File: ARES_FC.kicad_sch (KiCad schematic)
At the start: 65 parts, among them J1 SWD, J2 TYPE-C-31-M-12, J3 FC_M/P, J4 5V, J5 GND, J6 FC_RF, J7 Conn_01x04_Pin, J8 Conn_01x04_Pin, U1 STM32F401CCU6, U2 AMS1117-3.3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

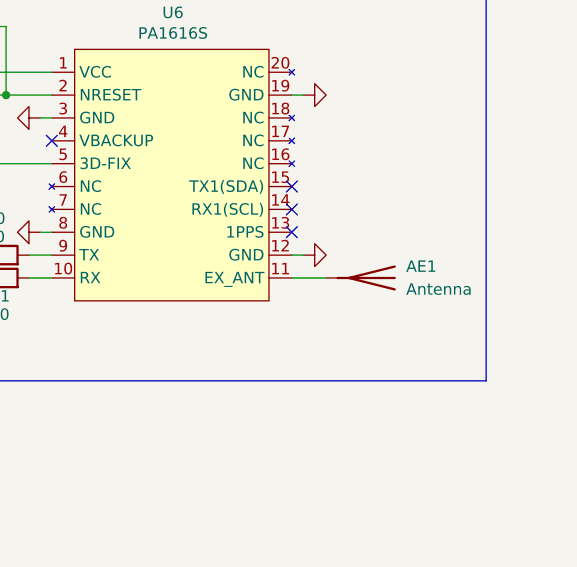
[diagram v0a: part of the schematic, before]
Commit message: added gps antenna shielding
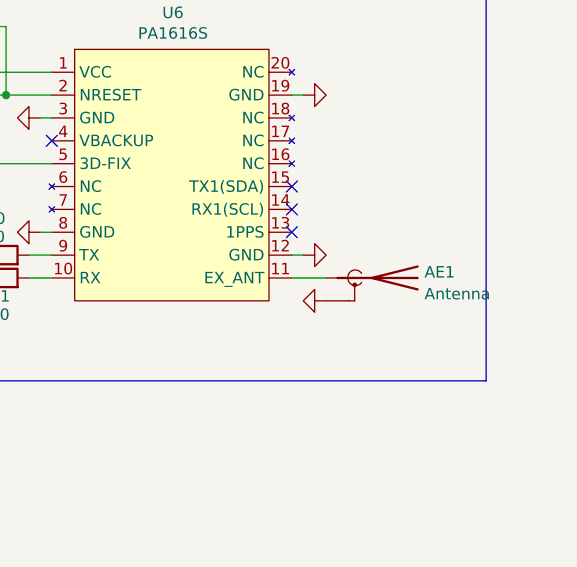
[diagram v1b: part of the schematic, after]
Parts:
- AE1: symbol Device:Antenna -> Device:Antenna_Shield
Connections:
- net GND: now also AE1.2 (Shield)
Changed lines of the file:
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@@
 	)
 	(symbol
-		(lib_id "Device:Antenna")
+		(lib_id "Device:Antenna_Shield")
 		(at 373.38 133.35 270)
 		(unit 1)
@@
 		(fields_autoplaced yes)
 		(property "Reference" "AE1"
-			(at 377.19 132.0799 90)
+			(at 379.222 132.7093 90)
 			(effects
 				(font
@@
 		)
 		(property "Value" "Antenna"
-			(at 377.19 134.6199 90)
+			(at 379.222 135.1336 90)
 			(effects
 				(font
@@
 		)
 		(property "Footprint" "Connector_Coaxial:U.FL_Molex_MCRF_73412-0110_Vertical"
-			(at 373.38 133.35 0)
+			(at 375.92 133.35 0)
 			(effects
 				(font
@@
 		)
 		(property "Datasheet" "~"
-			(at 373.38 133.35 0)
+			(at 375.92 133.35 0)
 			(effects
 				(font
@@
 			)
 		)
-		(property "Description" "Antenna"
+		(property "Description" "Antenna with extra pin for shielding"
 			(at 373.38 133.35 0)
 			(effects
@@
 		(pin "1"
 		)
+		(pin "2"
+		)
 		(instances
 			(project "ARES_FC"
@@
 					(unit 1)
 				)
+			)
+		)
+	)
+	(symbol
+		(lib_id "power:GND")
+		(at 368.3 135.89 270)
+		(unit 1)
+		(exclude_from_sim no)
+		(in_bom yes)
+		(on_board yes)
+		(dnp no)
+		(fields_autoplaced yes)
+		(property "Reference" "#PWR026"
+			(at 361.95 135.89 0)
+			(effects
+				(font
+					(size 1.27 1.27)
+				)
+				(hide yes)
+			)
+		)
+		(property "Value" "GND"
+			(at 363.22 135.89 0)
+			(effects
+				(font
+					(size 1.27 1.27)
+				)
+				(hide yes)
+			)
+		)
+		(property "Footprint" ""
+			(at 368.3 135.89 0)
+			(effects
+				(font
+					(size 1.27 1.27)
+				)
+				(hide yes)
+			)
+		)
+		(property "Datasheet" ""
+			(at 368.3 135.89 0)
+			(effects
+				(font
+					(size 1.27 1.27)
+				)
+				(hide yes)
+			)
+		)
+		(property "Description" ""
+			(at 368.3 135.89 0)
+			(effects
+				(font
+					(size 1.27 1.27)
+				)
+				(hide yes)
+			)
+		)
+		(pin "1"
+		)
+		(instances
+			(project "ARES_FC"
+				(path "/449acbee-2eeb-4316-a8e9-c26dd430524e"
+					(reference "#PWR026")
+					(unit 1)
+				)

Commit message: cleaned up schematic a bit
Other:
- note added: "BMP280 (Altimeter)"
- note added: "BNO055 (IMU)"
- note added: "PA1616S (GPS)"
- note added: "USB-C + LDO"
- note removed: "Altimeter"
- note removed: "BNO055"
- note removed: "GPS"
- note removed: "PA1616S"
- note removed: "USB-C OTG"
- moved on the sheet: D2, D3, R8, R9
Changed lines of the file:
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@@
 	(wire
 		(pts
-			(xy 132.588 186.69) (xy 132.588 189.23)
+			(xy 132.08 186.69) (xy 132.08 189.23)
 		)
 		(stroke
@@
 	(wire
 		(pts
-			(xy 132.588 196.85) (xy 132.588 199.39)
+			(xy 132.08 196.85) (xy 132.08 199.39)
 		)
 		(stroke
@@
 	(wire
 		(pts
-			(xy 132.588 172.974) (xy 132.588 179.07)
+			(xy 132.08 172.974) (xy 132.08 179.07)
 		)
 		(stroke
@@
 	(wire
 		(pts
-			(xy 137.668 196.85) (xy 137.668 199.39)
+			(xy 137.16 196.85) (xy 137.16 199.39)
 		)
 		(stroke
@@
 	(wire
 		(pts
-			(xy 137.668 172.974) (xy 137.668 179.07)
+			(xy 137.16 172.974) (xy 137.16 179.07)
 		)
 		(stroke
@@
 	(wire
 		(pts
-			(xy 137.668 186.69) (xy 137.668 189.23)
+			(xy 137.16 186.69) (xy 137.16 189.23)
 		)
 		(stroke
@@
 	(rectangle
 		(start 280.67 92.71)
-		(end 386.08 144.78)
+		(end 388.62 144.78)
 		(stroke
 			(width 0)
@@
 		)
 	)
-	(text "Altimeter"
+	(text "BMP280 (Altimeter)"
 		(exclude_from_sim no)
-		(at 295.402 70.866 0)
+		(at 300.228 70.866 0)
 		(effects
 			(font
@@
 		)
 	)
-	(text "PA1616S"
+	(text "PA1616S (GPS)"
 		(exclude_from_sim no)
-		(at 293.878 143.256 0)
+		(at 290.068 142.748 0)
 		(effects
 			(font
@@
 		)
 	)
-	(text "USB-C OTG"
+	(text "USB-C + LDO"
 		(exclude_from_sim no)
 		(at 178.562 90.678 0)
@@
 		)
 	)
-	(text "GPS"
-		(exclude_from_sim no)
-		(at 284.226 143.002 0)
-		(effects
-			(font
-				(size 1.27 1.27)
-			)
-		)
-	)
 	(text "UART CONNECTORS"
 		(exclude_from_sim no)
@@
 		)
 	)
-	(text "BNO055"
+	(text "BNO055 (IMU)"
 		(exclude_from_sim no)
 		(at 294.132 230.378 0)
@@
 	)
 	(label "LED_B"
-		(at 137.668 172.974 270)
+		(at 137.16 172.974 270)
 		(fields_autoplaced yes)
 		(effects
@@
 	)
 	(label "LED_G"
-		(at 132.588 172.974 270)
+		(at 132.08 172.974 270)
 		(fields_autoplaced yes)
 		(effects
@@
 	(symbol
 		(lib_id "power:GND")
-		(at 132.588 199.39 0)
+		(at 132.08 199.39 0)
 		(unit 1)
 		(exclude_from_sim no)
@@
 		(fields_autoplaced yes)
 		(property "Reference" "#PWR0136"
-			(at 132.588 205.74 0)
+			(at 132.08 205.74 0)
 			(effects
 				(font
@@
 		)
 		(property "Value" "GND"
-			(at 132.588 204.47 0)
+			(at 132.08 204.47 0)
 			(effects
 				(font
@@
 		)
 		(property "Footprint" ""
-			(at 132.588 199.39 0)
+			(at 132.08 199.39 0)
 			(effects
 				(font
@@
 		)
 		(property "Datasheet" ""
-			(at 132.588 199.39 0)
+			(at 132.08 199.39 0)
 			(effects
 				(font
@@
 		)
 		(property "Description" ""
-			(at 132.588 199.39 0)
+			(at 132.08 199.39 0)
 			(effects
 				(font
@@
 	(symbol
 		(lib_id "Device:R")
-		(at 132.588 193.04 0)
+		(at 132.08 193.04 0)
 		(unit 1)
 		(exclude_from_sim no)
@@
 		(on_board yes)
 		(dnp no)
-		(fields_autoplaced yes)
 		(property "Reference" "R8"
-			(at 134.366 192.2053 0)
+			(at 127.508 192.278 0)
 			(effects
 				(font
@@
 		)
 		(property "Value" "1k"
-			(at 134.366 194.7422 0)
+			(at 127.508 194.8149 0)
 			(effects
 				(font
@@
 		)
 		(property "Footprint" "Resistor_SMD:R_0402_1005Metric"
-			(at 130.81 193.04 90)
+			(at 130.302 193.04 90)
 			(effects
 				(font
@@
 		)
 		(property "Datasheet" "~"
-			(at 132.588 193.04 0)
+			(at 132.08 193.04 0)
 			(effects
 				(font
@@
 		)
 		(property "Description" ""
-			(at 132.588 193.04 0)
+			(at 132.08 193.04 0)
 			(effects
 				(font
@@
 		)
 		(property "LCSC Part" "C11702"
-			(at 132.588 193.04 0)
+			(at 132.08 193.04 0)
 			(effects
 				(font
@@
 	(symbol
 		(lib_id "Device:LED")
-		(at 132.588 182.88 90)
+		(at 132.08 182.88 90)
 		(unit 1)
 		(exclude_from_sim no)
@@
 		(dnp no)
 		(property "Reference" "D2"
-			(at 130.429 184.9028 90)
+			(at 126.746 181.864 90)
 			(effects
 				(font
@@
 		)
 		(property "Value" "LED"
-			(at 130.429 187.4397 90)
+			(at 126.746 184.4009 90)
 			(effects
 				(font
@@
 		)
 		(property "Footprint" "LED_SMD:LED_0603_1608Metric"
-			(at 132.588 182.88 0)
+			(at 132.08 182.88 0)
 			(effects
 				(font
@@
 		)
 		(property "Datasheet" "~"
-			(at 132.588 182.88 0)
+			(at 132.08 182.88 0)
 			(effects
 				(font
@@
 		)
 		(property "Description" ""
-			(at 132.588 182.88 0)
+			(at 132.08 182.88 0)
 			(effects
 				(font
@@
 		)
 		(property "LCSC Part" "C12624"
-			(at 132.588 182.88 0)
+			(at 132.08 182.88 0)
 			(effects
 				(font
@@
 	(symbol
 		(lib_id "Device:LED")
-		(at 137.668 182.88 90)
+		(at 137.16 182.88 90)
 		(unit 1)
 		(exclude_from_sim no)
@@
 		(dnp no)
 		(property "Reference" "D3"
-			(at 135.509 184.9028 90)
+			(at 138.938 181.6131 90)
 			(effects
 				(font
@@
 		)
 		(property "Value" "LED"
-			(at 135.509 187.4397 90)
+			(at 138.938 184.15 90)
 			(effects
 				(font
@@
 		)
 		(property "Footprint" "LED_SMD:LED_0603_1608Metric"
-			(at 137.668 182.88 0)
+			(at 137.16 182.88 0)
 			(effects
 				(font
@@
 		)
 		(property "Datasheet" "~"
-			(at 137.668 182.88 0)
+			(at 137.16 182.88 0)
 			(effects
 				(font
@@
 		)
 		(property "Description" ""
-			(at 137.668 182.88 0)
+			(at 137.16 182.88 0)
 			(effects
 				(font
@@
 		)
 		(property "LCSC Part" "C2288"
-			(at 137.668 182.88 0)
+			(at 137.16 182.88 0)
 			(effects
 				(font
@@
 	(symbol
 		(lib_id "power:GND")
-		(at 137.668 199.39 0)
+		(at 137.16 199.39 0)
 		(unit 1)
 		(exclude_from_sim no)
@@
 		(fields_autoplaced yes)
 		(property "Reference" "#PWR0140"
-			(at 137.668 205.74 0)
+			(at 137.16 205.74 0)
 			(effects
 				(font
@@
 		)
 		(property "Value" "GND"
-			(at 137.668 204.47 0)
+			(at 137.16 204.47 0)
 			(effects
 				(font
@@
 		)
 		(property "Footprint" ""
-			(at 137.668 199.39 0)
+			(at 137.16 199.39 0)
 			(effects
 				(font
@@
 		)
 		(property "Datasheet" ""
-			(at 137.668 199.39 0)
+			(at 137.16 199.39 0)
 			(effects
 				(font
@@
 		)
 		(property "Description" ""
-			(at 137.668 199.39 0)
+			(at 137.16 199.39 0)
 			(effects
 				(font
@@
 	(symbol
 		(lib_id "Device:R")
-		(at 137.668 193.04 0)
+		(at 137.16 193.04 0)
 		(unit 1)
 		(exclude_from_sim no)
@@
 		(fields_autoplaced yes)
 		(property "Reference" "R9"
-			(at 139.446 192.2053 0)
+			(at 138.938 192.2053 0)
 			(effects
 				(font
@@
 		)
 		(property "Value" "1k"
-			(at 139.446 194.7422 0)
+			(at 138.938 194.7422 0)
 			(effects
 				(font
@@
 		)
 		(property "Footprint" "Resistor_SMD:R_0402_1005Metric"
-			(at 135.89 193.04 90)
+			(at 135.382 193.04 90)
 			(effects
 				(font
@@
 		)
 		(property "Datasheet" "~"
-			(at 137.668 193.04 0)
+			(at 137.16 193.04 0)
 			(effects
 				(font
@@
 		)
 		(property "Description" ""
-			(at 137.668 193.04 0)
+			(at 137.16 193.04 0)
 			(effects
 				(font
@@
 		)
 		(property "LCSC Part" "C11702"
-			(at 137.668 193.04 0)
+			(at 137.16 193.04 0)
 			(effects
 				(font

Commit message: added gerbers & CPL for ordering
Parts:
- removed C14: 22uF, Capacitor_SMD:C_0805_2012Metric, symbol Device:C
- added C1: 22uF, Capacitor_SMD:C_0805_2012Metric, symbol Device:C
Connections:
- net +3.3V: now also C13.1
- net GND: now also C1.2
- net VBUS: now also C1.1; no longer C13.1
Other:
- note added: "LEDS"
- note added: "LOW-DROPOUT REGULATOR"
- note added: "MICROCONTROLLER (STM32)"
- note added: "RIBBON CONNECTORS"
- note added: "USB-C"
- note removed: "UART CONNECTORS"
- note removed: "USB-C + LDO"
- company: (none) -> Society for Advanced Rocket Propulsion
- title: (none) -> ARES Flight Computer
- moved on the sheet: C20, D2, D3, J1, J2, J4, J5, J7, J8, R1, R2, R7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

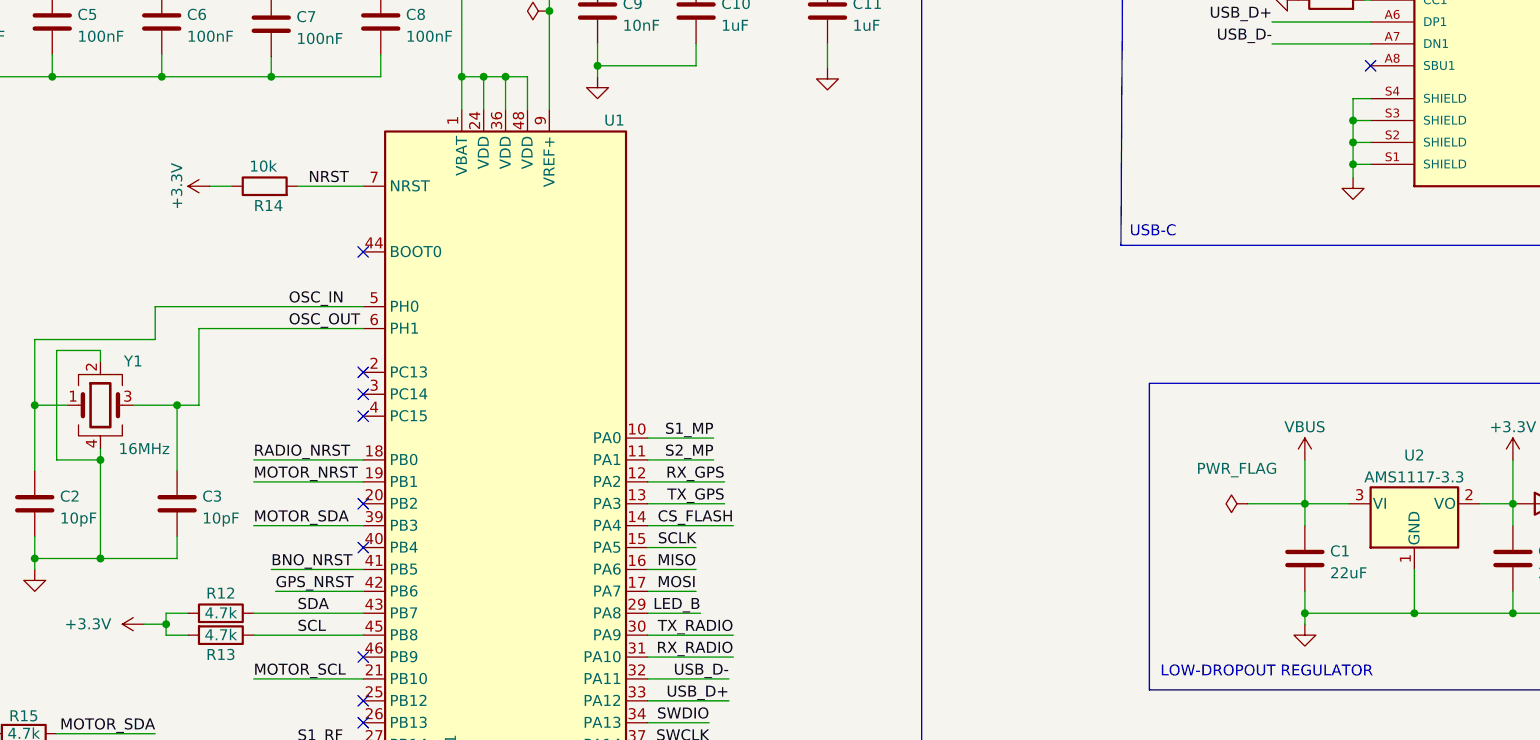
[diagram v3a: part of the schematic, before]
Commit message: removed pullup resistor on NRST
There is already an internal pullup according to the datasheet
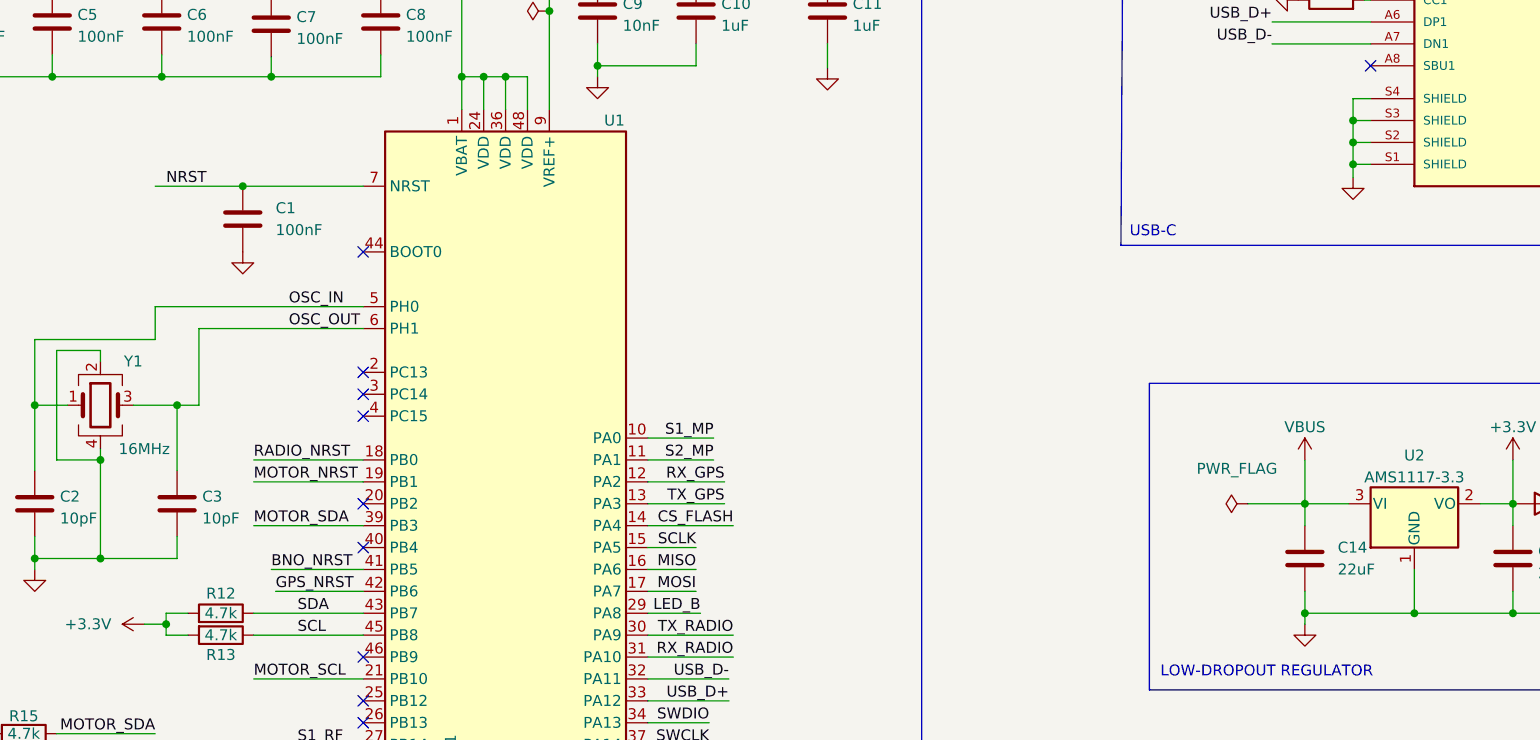
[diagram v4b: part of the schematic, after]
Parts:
- removed R14: 10k, Resistor_SMD:R_0402_1005Metric, symbol Device:R
- added C1: 100nF, Capacitor_SMD:C_0402_1005Metric, symbol Device:C
- renumbered C1 to C14
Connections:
- net GND: now also C1.1
- net NRST: now also C1.2
